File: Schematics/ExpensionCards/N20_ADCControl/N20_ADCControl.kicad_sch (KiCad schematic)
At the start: 36 parts

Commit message: Reworked N20/N21
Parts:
- C2001, C2002, C2003, C2004, C2005, C2006, C2008: footprint Capacitor_THT:C_Rect_L7.0mm_W2.0mm_P5.00mm -> Capacitor_THT:C_Disc_D5.0mm_W2.5mm_P5.00mm
- TP2001, TP2002, TP2003, TP2004, TP2005, TP2006, TP2007, TP2008, TP2009, TP2010, TP2011, TP2012, TP2013: footprint Connector_Pin:Pin_D1.0mm_L10.0mm -> Connector_Pin:Pin_D0.9mm_L10.0mm_W2.4mm_FlatFork
- renumbered K1 to X2001
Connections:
- net AZ: no longer D2003.12 (R)
- net _AZ renamed xAZ
- net xAZ: now also D2003.12 (R)
- net _C20 renamed xxC20
- net _EC20 renamed xEC20
- net _ECP renamed xECP
- net _ENC20 renamed xENC20
- net _ERD renamed xERD
- net _RDY renamed xRDY
- net _SCP renamed xSCP
- net _STD renamed xSTD
- net ~{CP} renamed x~{CP}
- net ~{_RD} renamed x~{RD}
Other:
- note added: "Signals for ADC: Ramp"
- note added: "Signals for ADC: UP, Autozero"
- note added: "Signals for counter (gated clockpulses, reset)"
- note added: "Signals for uP: counter-overflow"
- note added: "uP-counterpulses invert"
- note removed: "Carry20000"
- note removed: "Counter-pulse"
- note removed: "Ramp"
- company: (none) -> D. Kupers
- moved on the sheet: C2006, C2008, D2001A, D2001B, D2002A, D2002B, D2003A, D2003B, D2004A, D2004B, D2004C, D2004D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

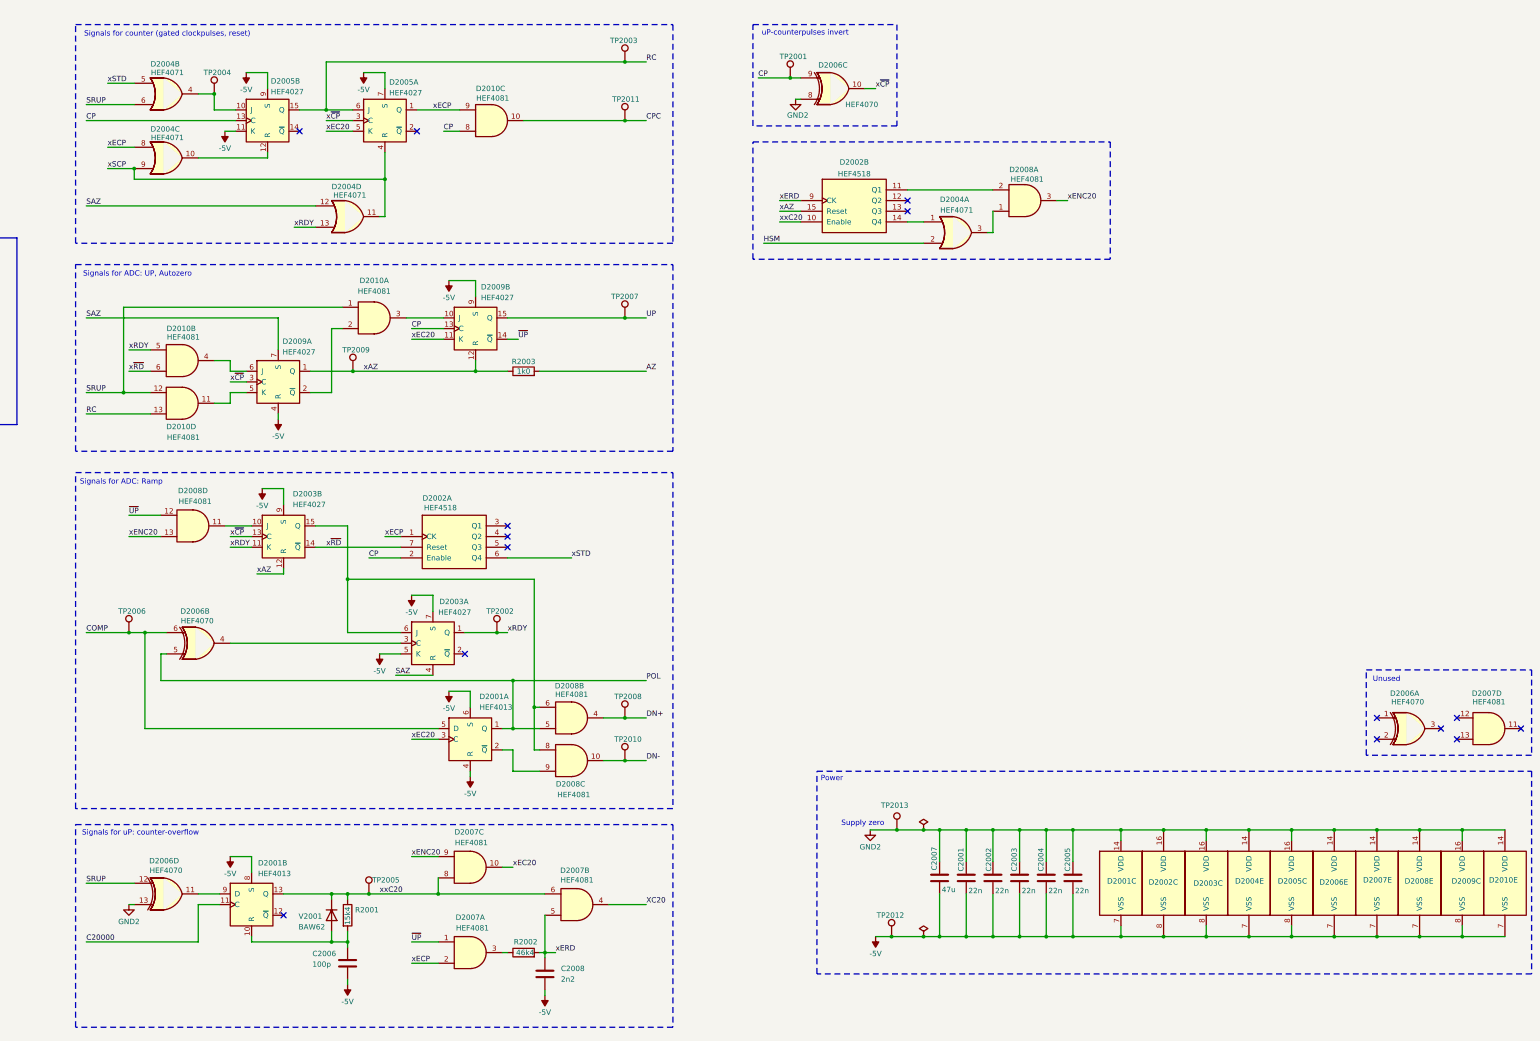
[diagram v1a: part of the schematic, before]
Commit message: Some more disassembly, optimize N20 schematics (naming of signals)
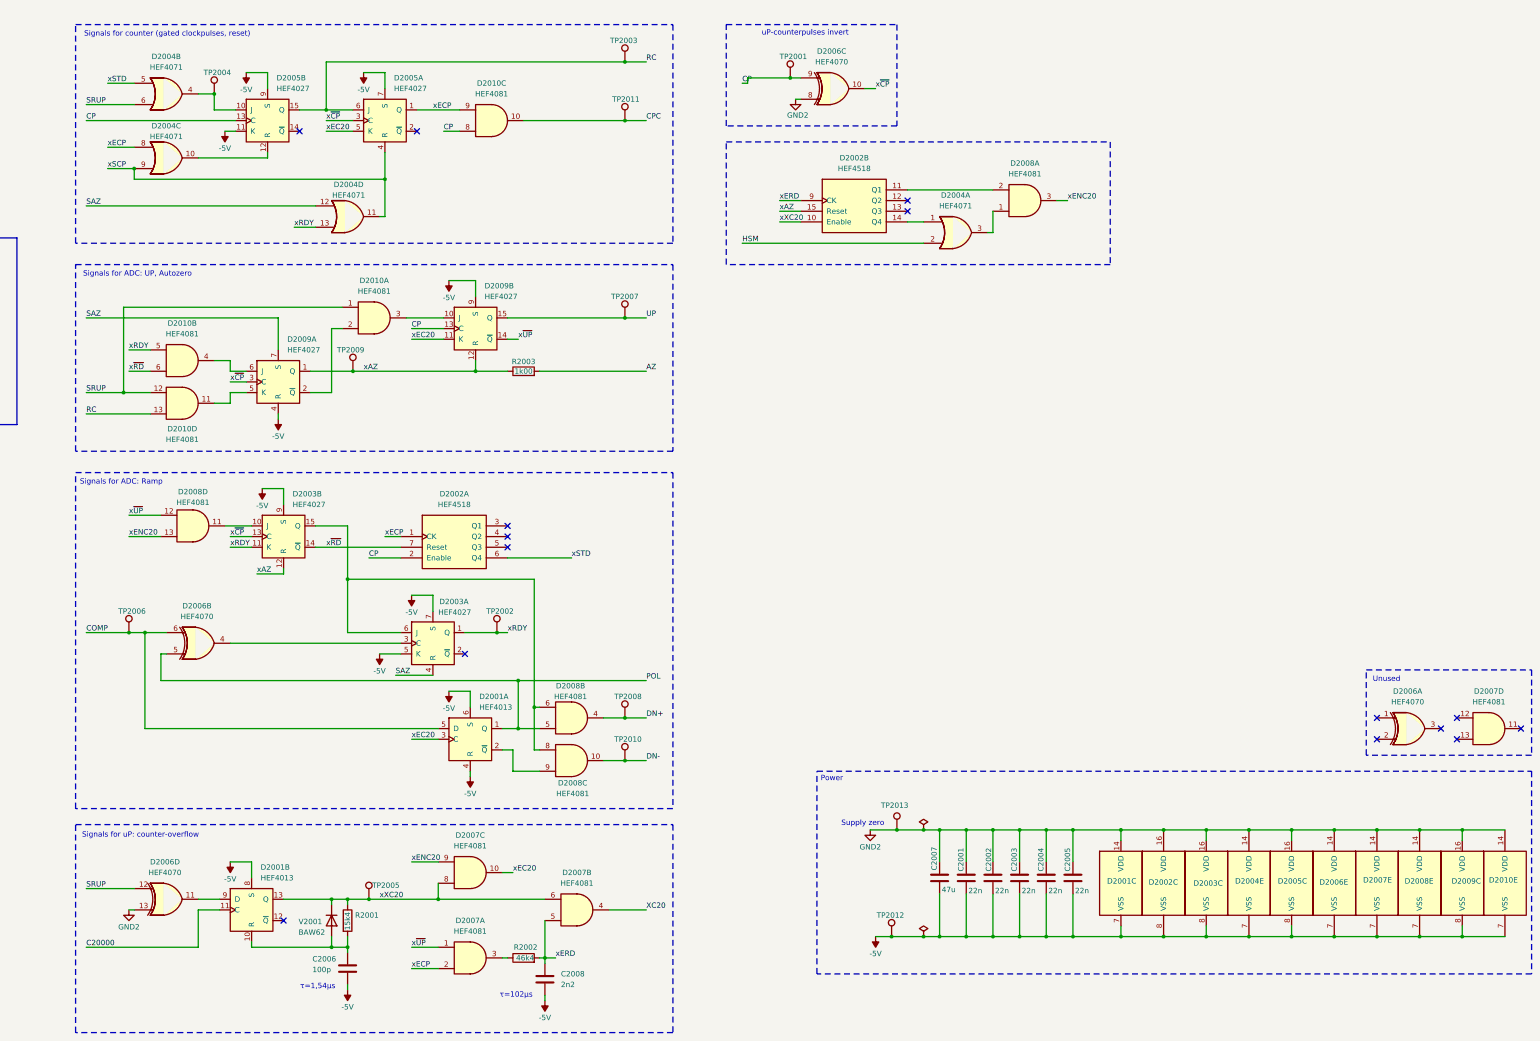
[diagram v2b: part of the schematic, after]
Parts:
- R2003: value 1k0 -> 1k00
- X2001: footprint PM2528:PM2528_RiserCardConnector -> Philips_PM2528:PM2528_RiserCardConnector
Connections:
- net xxC20 renamed xXC20
- net ~{UP} renamed x~{UP}
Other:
- note added: "τ=1,54μs"
- note added: "τ=102μs"
- moved on the sheet: C2006, C2008, D2001B, D2006D, D2007A, D2007B, D2007C, R2001, R2002, TP2005, V2001

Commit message: Small updates Some GPIB-analyzing-functions found.
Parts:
- X2001: footprint Philips_PM2528:PM2528_RiserCardConnector -> PhilipsPM2528:PM2528_RiserCardConnector
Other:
- moved on the sheet: C2006, C2008, D2001A, D2001B, D2002A, D2002B, D2003A, D2003B, D2004A, D2004B, D2004C, D2004D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

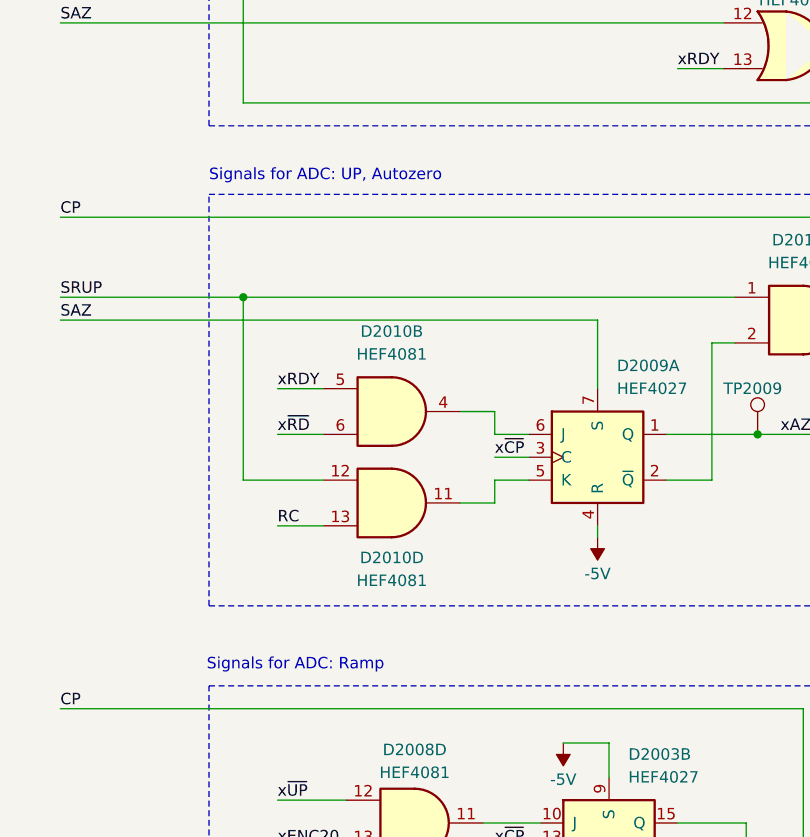
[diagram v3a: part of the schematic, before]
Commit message: Added LA-traces, some assembly-comments
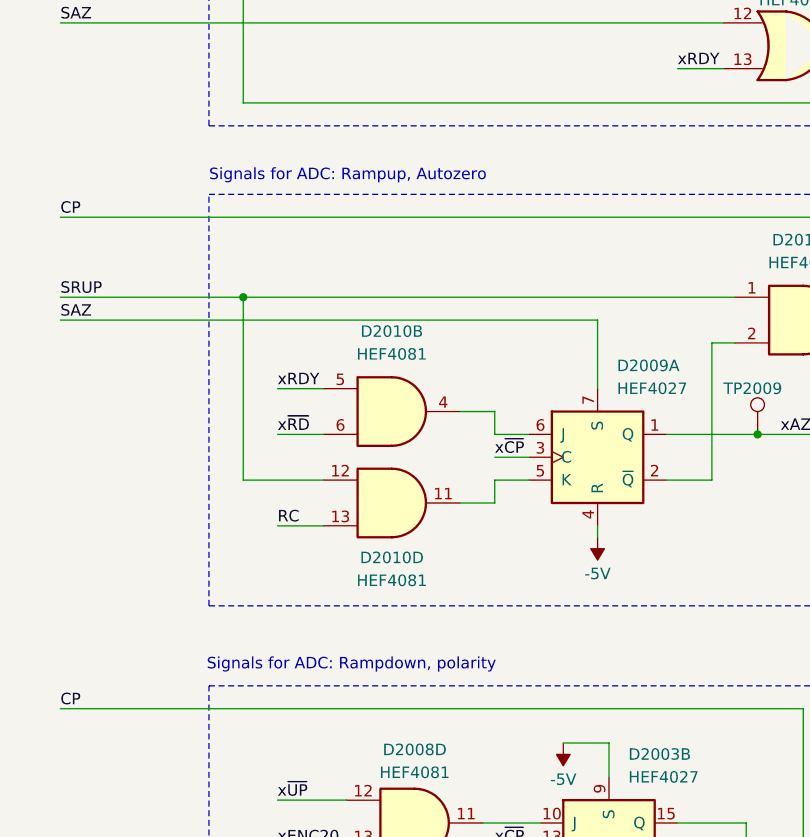
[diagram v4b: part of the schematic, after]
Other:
- note added: "Signals for ADC: Rampdown, polarity"
- note added: "Signals for ADC: Rampup, Autozero"
- note removed: "Signals for ADC: Ramp"
- note removed: "Signals for ADC: UP, Autozero"
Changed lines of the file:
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@@
 		)
 	)
-	(text "Signals for ADC: UP, Autozero"
+	(text "Signals for ADC: Rampup, Autozero"
 		(exclude_from_sim no)
 		(at 63.5 80.518 0)
@@
 		)
 	)
-	(text "Signals for ADC: Ramp"
+	(text "Signals for ADC: Rampdown, polarity"
 		(exclude_from_sim no)
 		(at 63.246 134.874 0)

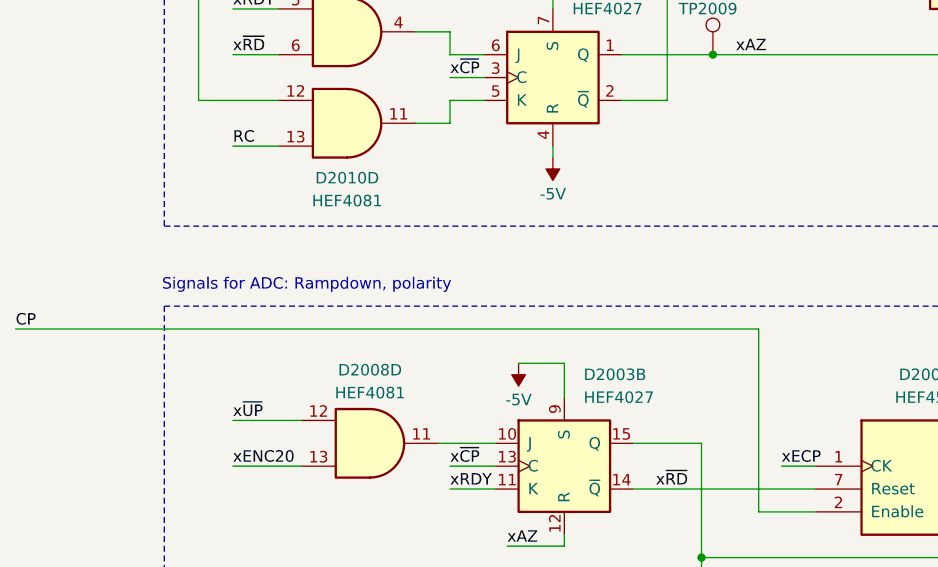
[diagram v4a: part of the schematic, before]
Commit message: Added N20 deepdive
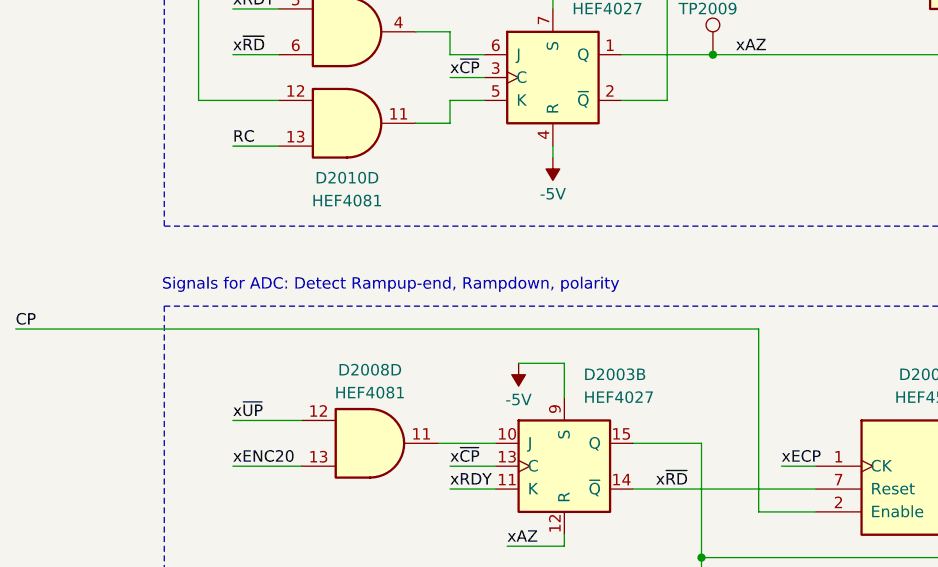
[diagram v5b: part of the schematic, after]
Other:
- note added: "Signals for ADC: Detect Rampup-end, Rampdown, polarity"
- note removed: "Signals for ADC: Rampdown, polarity"
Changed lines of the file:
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@@
 		)
 	)
-	(text "Signals for ADC: Rampdown, polarity"
+	(text "Signals for ADC: Detect Rampup-end, Rampdown, polarity"
 		(exclude_from_sim no)
 		(at 63.246 134.874 0)
